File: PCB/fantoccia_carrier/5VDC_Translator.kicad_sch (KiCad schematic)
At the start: 2 parts, among them U2 TXS0108EPWR, U3 TXS0108EPWR

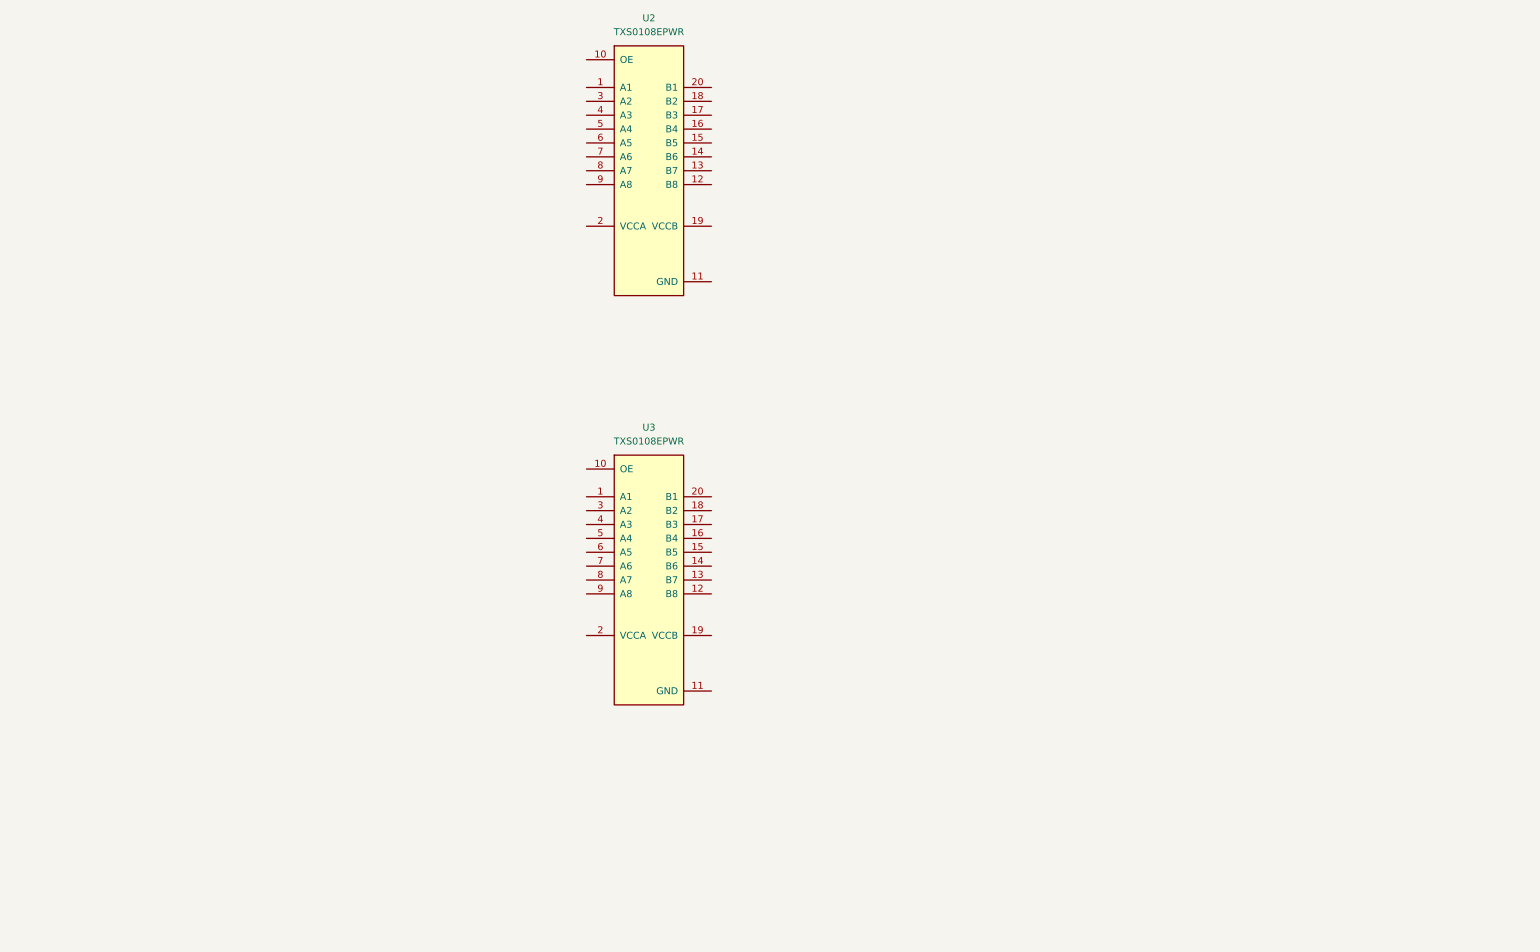
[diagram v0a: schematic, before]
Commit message: PCB Created
Schematic mostly finished, just need to figure out pinning and add more TVS protection. Created PCB might need to tweak footprint.
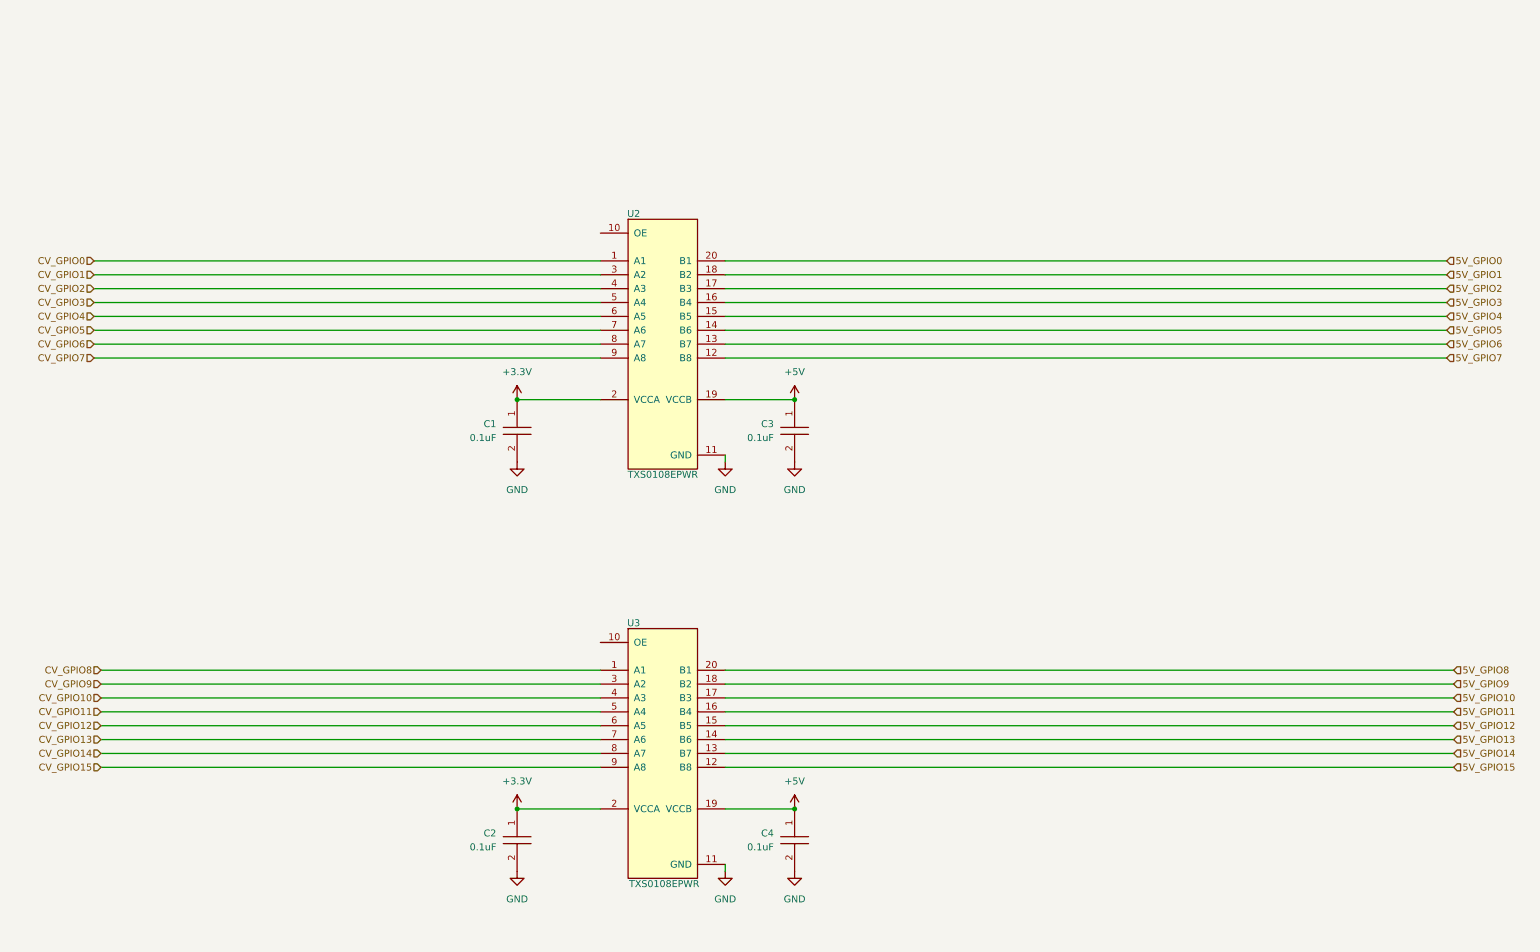
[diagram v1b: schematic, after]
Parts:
- added C1, C2, C3, C4: CGA3E2X7R1H104K080AA, AVR-KiCAD-Lib-Capacitors:C0603, symbol AVR-KiCAD-Lib-Capacitors:CGA3E2X7R1H104K080AA
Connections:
- net CV_GPIO8: now reaches U3.1 (A1)
- net GND: now reaches U3.11 (GND)
- net GND: now also U2.11 (GND), C1.2, C2.2, C3.2, C4.2
- net 5V_GPIO15: now reaches U3.12 (B8)
- net 5V_GPIO14: now reaches U3.13 (B7)
- net 5V_GPIO13: now reaches U3.14 (B6)
- net 5V_GPIO12: now reaches U3.15 (B5)
- net 5V_GPIO11: now reaches U3.16 (B4)
- net 5V_GPIO10: now reaches U3.17 (B3)
- net 5V_GPIO9: now reaches U3.18 (B2)
- net +5V: now reaches U3.19 (VCCB)
- net +5V: now also U2.19 (VCCB), C3.1, C4.1
- net +3.3V: now reaches U3.2 (VCCA)
- net +3.3V: now also U2.2 (VCCA), C1.1, C2.1
- net 5V_GPIO8: now reaches U3.20 (B1)
- net CV_GPIO9: now reaches U3.3 (A2)
- net CV_GPIO10: now reaches U3.4 (A3)
- net CV_GPIO11: now reaches U3.5 (A4)
- net CV_GPIO12: now reaches U3.6 (A5)
- net CV_GPIO13: now reaches U3.7 (A6)
- net CV_GPIO14: now reaches U3.8 (A7)
- net CV_GPIO15: now reaches U3.9 (A8)
- net CV_GPIO0: now reaches U2.1 (A1)
- net 5V_GPIO7: now reaches U2.12 (B8)
- net 5V_GPIO6: now reaches U2.13 (B7)
- net 5V_GPIO5: now reaches U2.14 (B6)
- net 5V_GPIO4: now reaches U2.15 (B5)
- net 5V_GPIO3: now reaches U2.16 (B4)
- net 5V_GPIO2: now reaches U2.17 (B3)
- net 5V_GPIO1: now reaches U2.18 (B2)
- net 5V_GPIO0: now reaches U2.20 (B1)
- net CV_GPIO1: now reaches U2.3 (A2)
- net CV_GPIO2: now reaches U2.4 (A3)
- net CV_GPIO3: now reaches U2.5 (A4)
- net CV_GPIO4: now reaches U2.6 (A5)
- net CV_GPIO5: now reaches U2.7 (A6)
- net CV_GPIO6: now reaches U2.8 (A7)
- net CV_GPIO7: now reaches U2.9 (A8)
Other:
- moved on the sheet: U2, U3

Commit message: PCB progress and feature updates
Added another bank of 5V channels. PCB layout figured out, board shape defined. 3D model added to STM32 evaluation kit. Now just need to determine pinout and add protection circuitry to pins.
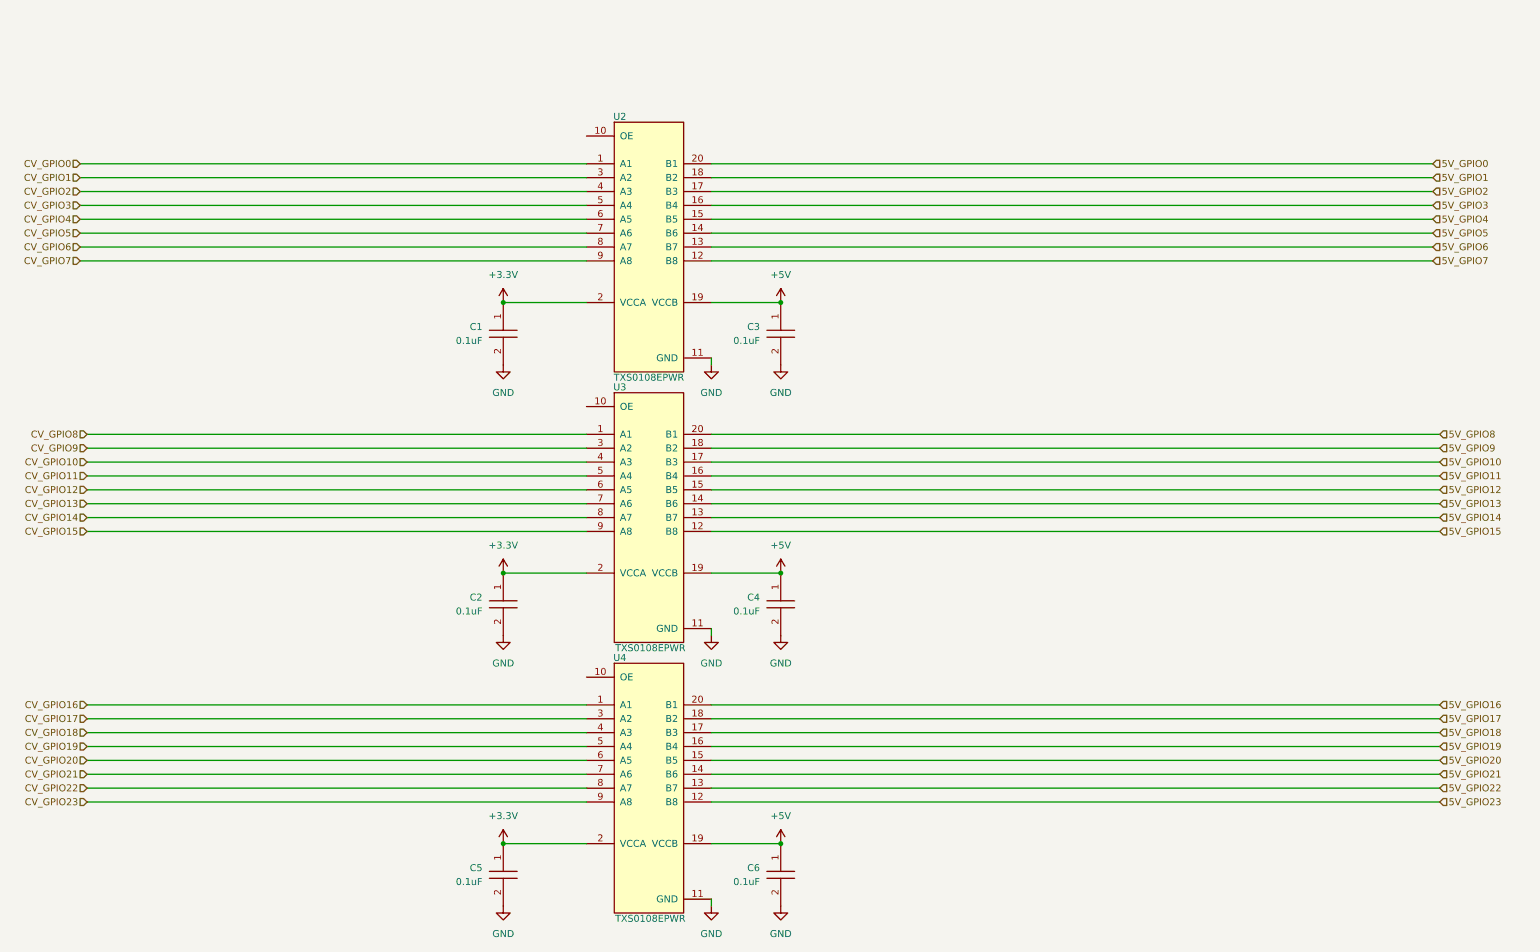
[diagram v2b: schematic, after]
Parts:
- added C5, C6: CGA3E2X7R1H104K080AA, AVR-KiCAD-Lib-Capacitors:C0603, symbol AVR-KiCAD-Lib-Capacitors:CGA3E2X7R1H104K080AA
- added U4: TXS0108EPWR, AVR-KiCAD-Lib-ICs:SOP65P640X120-20N, symbol AVR-KiCAD-Lib-ICs:TXS0108EPWR
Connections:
- net +3.3V: now also C5.1, U4.2 (VCCA)
- net +5V: now also C6.1, U4.19 (VCCB)
- net GND: now also C5.2, C6.2, U4.11 (GND)
- new net 5V_GPIO16: U4.20 (B1)
- new net 5V_GPIO17: U4.18 (B2)
- new net 5V_GPIO18: U4.17 (B3)
- new net 5V_GPIO19: U4.16 (B4)
- new net 5V_GPIO20: U4.15 (B5)
- new net 5V_GPIO21: U4.14 (B6)
- new net 5V_GPIO22: U4.13 (B7)
- new net 5V_GPIO23: U4.12 (B8)
- new net CV_GPIO16: U4.1 (A1)
- new net CV_GPIO17: U4.3 (A2)
- new net CV_GPIO18: U4.4 (A3)
- new net CV_GPIO19: U4.5 (A4)
- new net CV_GPIO20: U4.6 (A5)
- new net CV_GPIO21: U4.7 (A6)
- new net CV_GPIO22: U4.8 (A7)
- new net CV_GPIO23: U4.9 (A8)
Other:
- moved on the sheet: C1, C2, C3, C4, U2, U3
